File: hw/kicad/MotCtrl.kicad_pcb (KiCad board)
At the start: 4 copper layers, 76.7 x 44.5 mm, 145 parts, among them P1 CONN_01X06, P2 CONN_01X03, P3 CONN_02X05, P4 CONN_01X05, Q1 FDBL0110N60, Q2 FDBL0110N60, Q3 FDBL0110N60, Q4 FDBL0110N60, Q5 FDBL0110N60, Q6 FDBL0110N60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

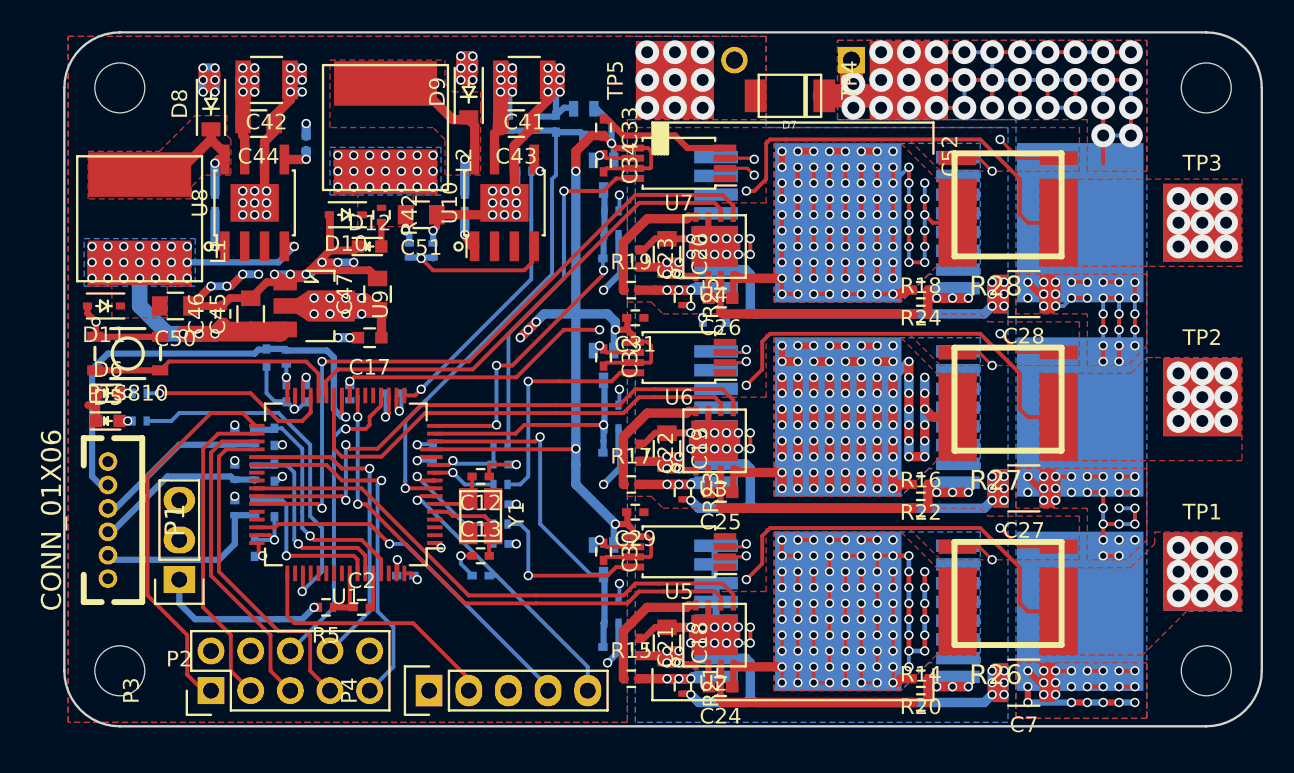
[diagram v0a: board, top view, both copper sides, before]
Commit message: Added current sense voltage reference as reparate net again
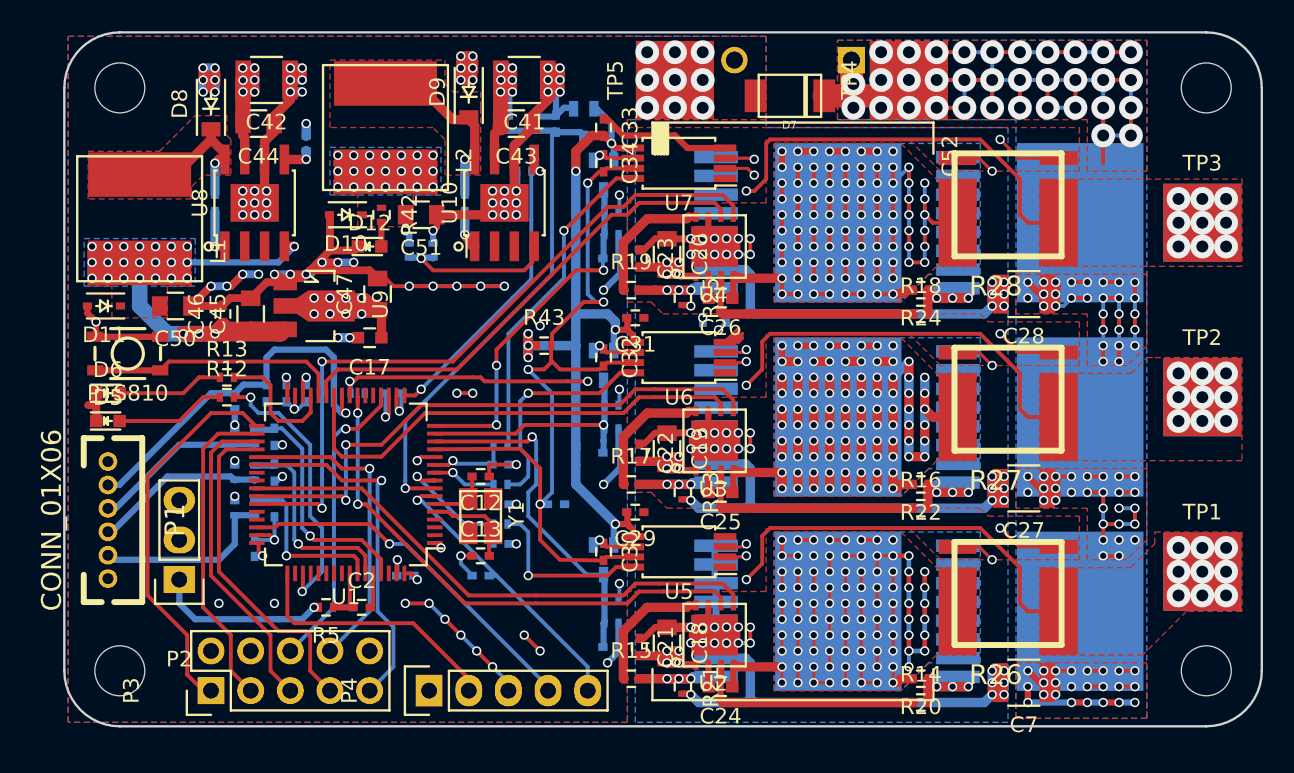
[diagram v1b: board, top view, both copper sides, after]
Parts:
- added R43: 0R, Resistors_SMD:R_0402, F.Cu at (156.5, 127.3)
- R12, R13: moved to F.Cu
- moved C9 8.54 mm to (157.2, 137.4), turned to 0 degrees
- moved R12 5.79 mm to (136.1, 130.6)
- moved R13 5.68 mm to (136.1, 129.3)
- moved R8 4.33 mm to (136.7, 130.8)
- moved C6 2.29 mm to (138.7, 130.3)
- moved R3 0.51 mm to (144.5, 130.3), turned to 0 degrees
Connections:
- C30 pad 2: +3V3 -> /Power FET/I_SENSE_V_REF
- C32 pad 2: +3V3 -> /Power FET/I_SENSE_V_REF
- C34 pad 2: +3V3 -> /Power FET/I_SENSE_V_REF
- C9 pad 1: +3V3 -> /Power FET/I_SENSE_V_REF
- U1 pad 13: +3V3 -> /Power FET/I_SENSE_V_REF
- U5 pad 7: +3V3 -> /Power FET/I_SENSE_V_REF
- U6 pad 7: +3V3 -> /Power FET/I_SENSE_V_REF
- U7 pad 7: +3V3 -> /Power FET/I_SENSE_V_REF
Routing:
- net /Power FET/I_SENSE_V_REF: track 0.00 -> 53.7 mm, vias 0 -> 4
- net GND: track 353.6 -> 402.6 mm, vias 139 -> 157
- net +3V3: track 151.3 -> 127.0 mm, vias 26 -> 24
- net Net-(D5-Pad2): track 0.83 -> 7.05 mm, vias 1 -> 0
- net Net-(D6-Pad2): track 0.83 -> 6.84 mm, vias 1 -> 0
- net /Microcontroller/MOT_TEMP: track 30.8 -> 25.1 mm
- net /Microcontroller/LED_R: track 22.9 -> 17.9 mm, vias 1 -> 2
- net /Microcontroller/LED_G: track 12.6 -> 8.44 mm, vias 1 -> 0
- net Net-(R34-Pad1): track 23.2 -> 21.7 mm
- net +5V: track 83.8 -> 84.8 mm
- net /Microcontroller/BOARD_TEMP: track 27.9 -> 28.5 mm

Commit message: Silkscreen placed correctly
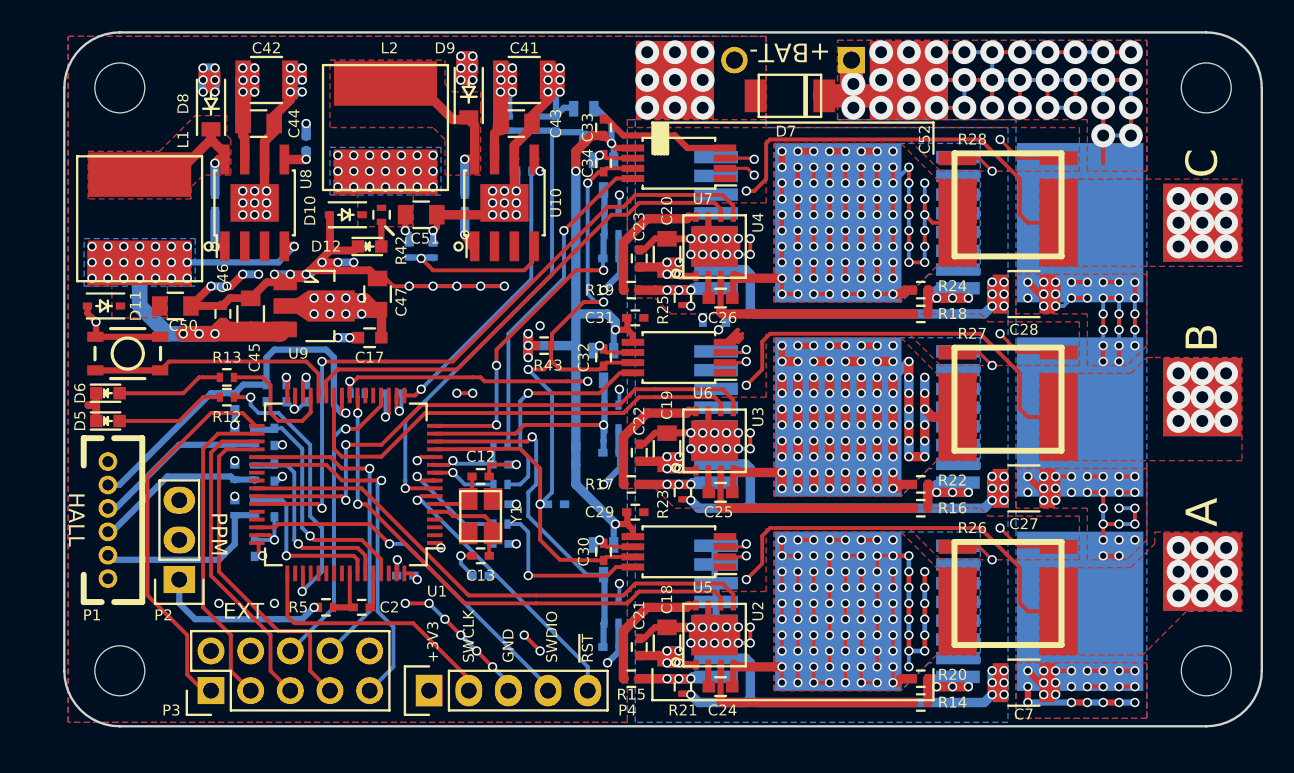
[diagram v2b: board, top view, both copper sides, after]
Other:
- board text added: "+3V3"
- board text added: "+5V"
- board text added: "+BAT-"
- board text added: "-BAT+"
- board text added: "A"
- board text added: "B"
- board text added: "C"
- board text added: "EXT"
- board text added: "GND"
- board text added: "H1"
- board text added: "H2"
- board text added: "H3"
- board text added: "HALL"
- board text added: "MotCtrl"
- board text added: "PPM"
- board text added: "REV A"
- board text added: "SWCLK"
- board text added: "SWDIO"
- board text added: "TEMP"
- board text added: "osannolik"
- board text added: "~RST~"

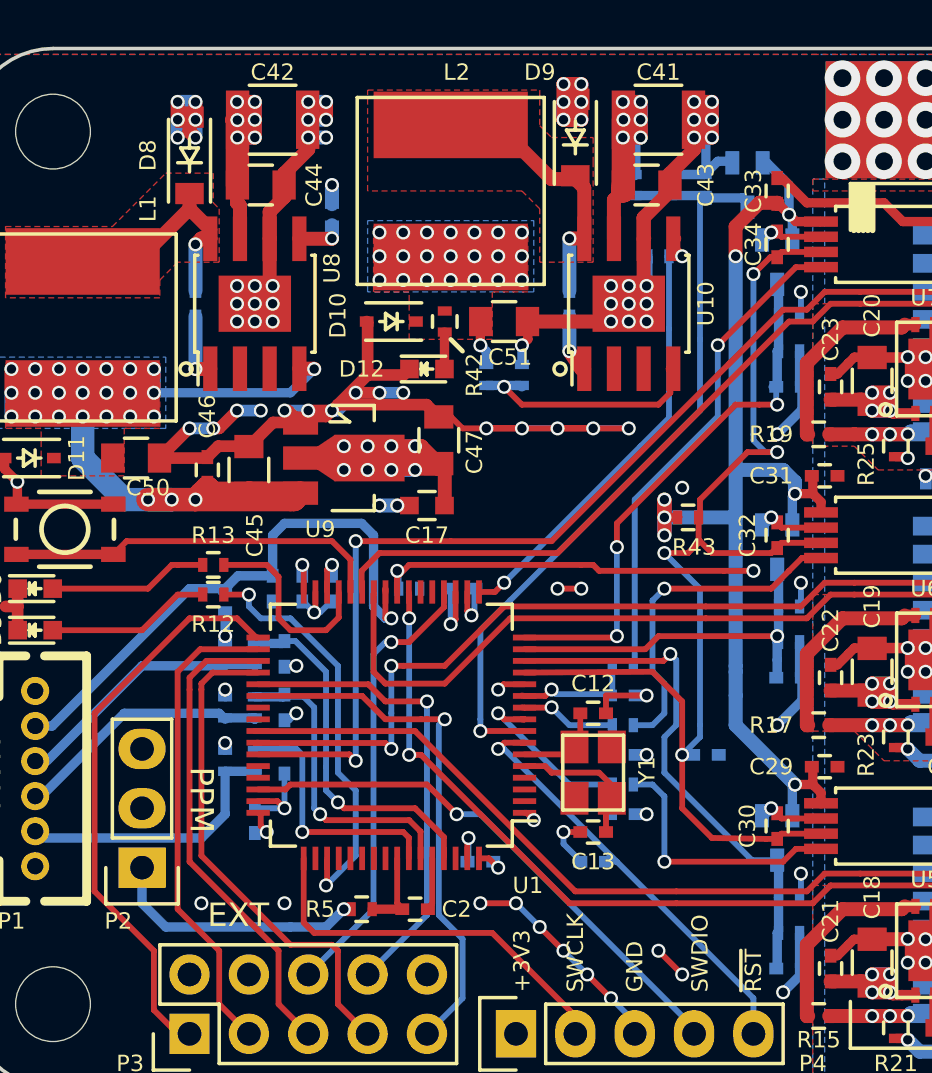
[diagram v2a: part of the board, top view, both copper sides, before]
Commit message: Add test pads
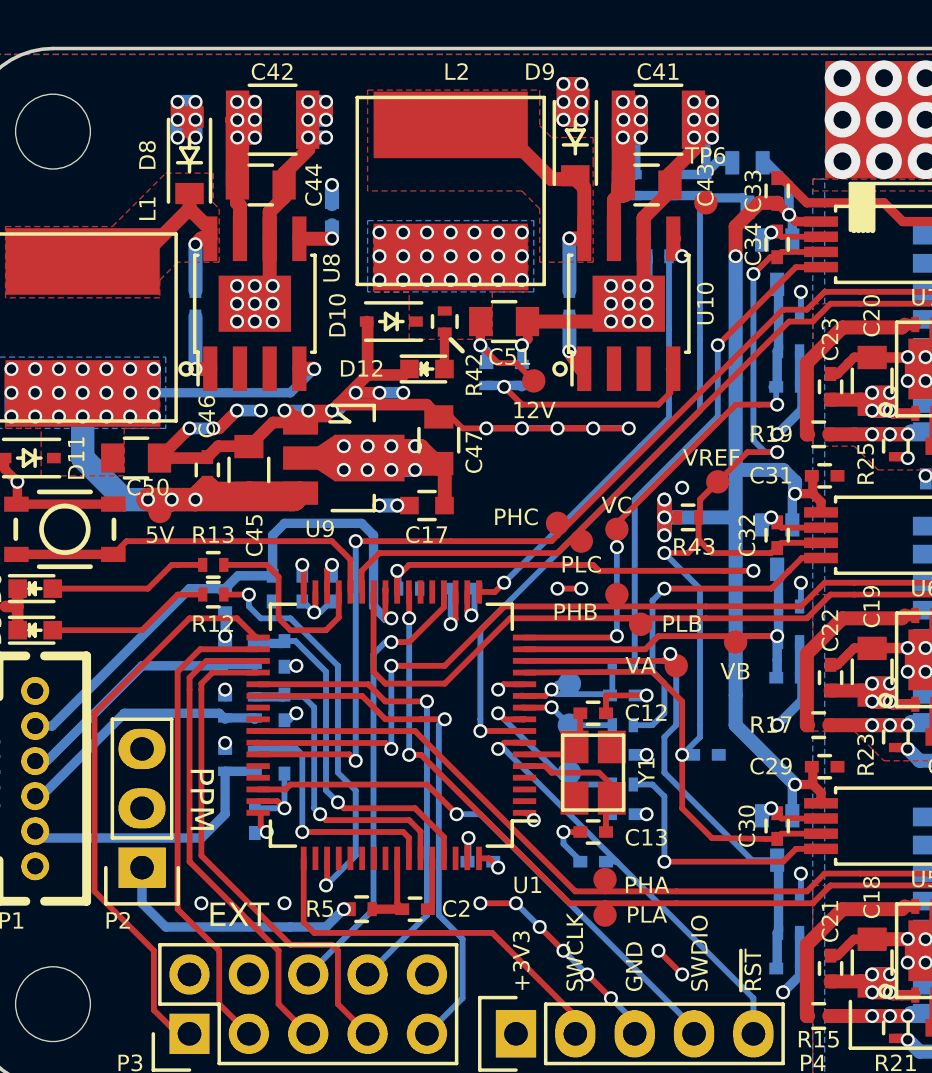
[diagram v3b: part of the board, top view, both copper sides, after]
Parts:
- added TP10: IB, Measurement_Points:Measurement_Point_Round-SMD-Pad_Small, B.Cu at (151.4, 136.1)
- added TP11: VC, Measurement_Points:Measurement_Point_Round-SMD-Pad_Small, F.Cu at (153.4, 127.8)
- added TP12: IC, Measurement_Points:Measurement_Point_Round-SMD-Pad_Small, B.Cu at (151.4, 134.4)
- added TP13: VREF, Measurement_Points:Measurement_Point_Round-SMD-Pad_Small, F.Cu at (157.7, 125.7)
- added TP14: PHA, Measurement_Points:Measurement_Point_Round-SMD-Pad_Small, F.Cu at (152.9, 142.7)
- added TP15: PHB, Measurement_Points:Measurement_Point_Round-SMD-Pad_Small, F.Cu at (153.4, 130.6)
- added TP16: PHC, Measurement_Points:Measurement_Point_Round-SMD-Pad_Small, F.Cu at (150.9, 127.5)
- added TP17: PLA, Measurement_Points:Measurement_Point_Round-SMD-Pad_Small, F.Cu at (152.9, 144.3)
- added TP18: PLB, Measurement_Points:Measurement_Point_Round-SMD-Pad_Small, F.Cu at (154.4, 131.8)
- added TP19: PLC, Measurement_Points:Measurement_Point_Round-SMD-Pad_Small, F.Cu at (151.9, 128.3)
- added TP20: 5V, Measurement_Points:Measurement_Point_Round-SMD-Pad_Small, F.Cu at (133.9, 127.0)
- added TP21: 12V, Measurement_Points:Measurement_Point_Round-SMD-Pad_Small, F.Cu at (149.9, 121.4)
- added TP6: BAT_SENSE, Measurement_Points:Measurement_Point_Round-SMD-Pad_Small, F.Cu at (157.2, 113.8)
- added TP7: VA, Measurement_Points:Measurement_Point_Round-SMD-Pad_Small, F.Cu at (156.0, 133.6)
- added TP8: IA, Measurement_Points:Measurement_Point_Round-SMD-Pad_Small, B.Cu at (151.4, 138.2)
- added TP9: VB, Measurement_Points:Measurement_Point_Round-SMD-Pad_Small, F.Cu at (158.5, 132.6)
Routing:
- net +12V: track 65.5 -> 68.4 mm
- net /Microcontroller/V_EMF_SENSE_B: track 16.2 -> 18.2 mm
- net /Power FET/I_SENSE_V_REF: track 53.7 -> 55.1 mm
- net /Microcontroller/I_SENS_C: track 5.52 -> 6.83 mm
- net /Microcontroller/PWM_L_B: track 30.6 -> 31.9 mm
- net +5V: track 84.8 -> 85.5 mm
- net /Microcontroller/V_EMF_SENSE_A: track 22.9 -> 23.5 mm
- net /Microcontroller/PWM_L_C: track 31.6 -> 32.1 mm
- net /Microcontroller/PWM_H_A: track 35.0 -> 35.5 mm
- net /Microcontroller/I_SENS_A: track 8.94 -> 9.45 mm
- net /Microcontroller/PWM_H_C: track 45.4 -> 46.0 mm
- net /Microcontroller/PWM_L_A: track 34.1 -> 34.6 mm
- net /Microcontroller/PWM_H_B: track 36.9 -> 37.4 mm
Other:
- board text added: "2016"

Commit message: Revision A sent to fab
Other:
- board text added: "Jonas A"
- board text removed: "osannolik"
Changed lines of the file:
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@@
     (links 379)
     (no_connects 1)
-    (area 125.654999 107.112999 202.513001 151.713001)
+    (area 122.609002 105.867 216.320572 159.164001)
     (thickness 1.6)
     (drawings 60)
@@
     (visible_elements FFFEFFFF)
     (pcbplotparams
-      (layerselection 0x00030_80000001)
+      (layerselection 0x010f0_80000007)
       (usegerberextensions false)
       (excludeedgelayer true)
@@
       (psa4output false)
       (plotreference true)
-      (plotvalue true)
+      (plotvalue false)
       (plotinvisibletext false)
       (padsonsilk false)
       (subtractmaskfromsilk false)
-      (outputformat 1)
+      (outputformat 4)
       (mirror false)
-      (drillshape 1)
+      (drillshape 0)
       (scaleselection 1)
-      (outputdirectory ""))
+      (outputdirectory output/pdf/))
   )
   (net 0 "")
@@
   (gr_line (start 128.27 132.842) (end 128.27 131.318) (angle 90) (layer B.Mask) (width 0.2))
   (gr_line (start 129.794 126.746) (end 129.794 132.842) (angle 90) (layer B.Mask) (width 0.2))
-  (gr_text osannolik (at 128.524 119.126 270) (layer B.Mask)
+  (gr_text "Jonas A" (at 128.524 119.126 270) (layer B.Mask)
     (effects (font (size 0.7 0.7) (thickness 0.15)) (justify left mirror))
   )
